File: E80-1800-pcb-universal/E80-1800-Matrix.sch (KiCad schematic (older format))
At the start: 276 parts

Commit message: finished pcb layout, added silk labels
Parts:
- D2001, D2002, D2003, D2004, D2005, D2006, D2007, D2008, D2009, D2010, D2011, D2012, D2013, D2014, D2015, D2016, D2017, D2018, D2019, D2020, D2021, D2022, D2023, D2024, D2025, D2026, D2027, D2028, D2029, D2030, D2031, D2032, D2033, D2034, D2035, D2036, D2037, D2038, D2039, D2040, D2041, D2042, D2043, D2044, D2045, D2046, D2047, D2048, D2049, D2050, D2051, D2052, D2053, D2054: LCSC (none) -> C68978
- R2001, R2002, R2003, R2004, R2005, R2006, R2007, R2008, R2009, R2010, R2011, R2012, R2013, R2014, R2015, R2016, R2017, R2018, R2019, R2020, R2021, R2022, R2023, R2024, R2025, R2026, R2027, R2028, R2029, R2030, R2031, R2032, R2033, R2034, R2035, R2036, R2037, R2038, R2039, R2040, R2041, R2042, R2043, R2044, R2045, R2046, R2047, R2048, R2049, R2050, R2051, R2052, R2053, R2054, R2055, R2056, R2057, R2058, R2059, R2060, R2061, R2062, R2063, R2064, R2065, R2066, R2067, R2068, R2069, R2070, R2071, R2072, R2073, R2074, R2075, R2076, R2077, R2078, R2079, R2080, R2081, R2082, R2083, R2084, R2085, R2086, R2087, R2088, R2089, R2090, R2091, R2092, R2093, R2094, R2095, R2096, R2097, R2098, R2099, R2100, R2101, R2102, R2103, R2104, R2105, R2106, R2107: LCSC (none) -> C23204

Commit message: improved mounting holes
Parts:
- renumbered D2007 to D10, D2008 to D11, D2009 to D12, D2010 to D13, D2011 to D14, D2012 to D15, D2013 to D16, D2014 to D17, D2015 to D18, D2016 to D19, D2017 to D20, D2018 to D21, D2019 to D22, D2020 to D23, D2021 to D24, D2022 to D25, D2023 to D26, D2024 to D27, D2025 to D28, D2026 to D29, D2027 to D30, D2028 to D31, D2029 to D32, D2030 to D33, D2031 to D34, D2032 to D35, D2033 to D36, D2034 to D37, D2035 to D38, D2036 to D39, D2001 to D4, D2037 to D40, D2038 to D41, D2039 to D42, D2040 to D43, D2041 to D44, D2042 to D45, D2043 to D46, D2044 to D47, D2045 to D48, D2046 to D49, D2002 to D5, D2047 to D50, D2048 to D51, D2049 to D52, D2050 to D53, D2051 to D54, D2052 to D55, D2053 to D56, D2054 to D57, D2003 to D6, D2004 to D7, D2005 to D8, D2006 to D9, MX2001 to MX1, MX2010 to MX10, MX2100 to MX100, MX2101 to MX101, MX2102 to MX102, MX2103 to MX103, MX2104 to MX104, MX2105 to MX105, MX2106 to MX106, MX2107 to MX107, MX2108 to MX108, MX2109 to MX109, MX2011 to MX11, MX2110 to MX110, MX2111 to MX111, MX2112 to MX112, MX2113 to MX113, MX2114 to MX114, MX2115 to MX115, MX2012 to MX12, MX2013 to MX13, MX2014 to MX14, MX2015 to MX15, MX2016 to MX16, MX2017 to MX17, MX2018 to MX18, MX2019 to MX19, MX2002 to MX2, MX2020 to MX20, MX2021 to MX21, MX2022 to MX22, MX2023 to MX23, MX2024 to MX24, MX2025 to MX25, MX2026 to MX26, MX2027 to MX27, MX2028 to MX28, MX2029 to MX29, MX2003 to MX3, MX2030 to MX30, MX2031 to MX31, MX2032 to MX32, MX2033 to MX33, MX2034 to MX34, MX2035 to MX35, MX2036 to MX36, MX2037 to MX37, MX2038 to MX38, MX2039 to MX39, MX2004 to MX4, MX2040 to MX40, MX2041 to MX41, MX2042 to MX42, MX2043 to MX43, MX2044 to MX44, MX2045 to MX45, MX2046 to MX46, MX2047 to MX47, MX2048 to MX48, MX2049 to MX49, MX2005 to MX5, MX2050 to MX50, MX2051 to MX51, MX2052 to MX52, MX2053 to MX53, MX2054 to MX54, MX2055 to MX55, MX2056 to MX56, MX2057 to MX57, MX2058 to MX58, MX2059 to MX59, MX2006 to MX6, MX2060 to MX60, MX2061 to MX61, MX2062 to MX62, MX2063 to MX63, MX2064 to MX64, MX2065 to MX65, MX2066 to MX66, MX2067 to MX67, MX2068 to MX68, MX2069 to MX69, MX2007 to MX7, MX2070 to MX70, MX2071 to MX71, MX2072 to MX72, MX2073 to MX73, MX2074 to MX74, MX2075 to MX75, MX2076 to MX76, MX2077 to MX77, MX2078 to MX78, MX2079 to MX79, MX2008 to MX8, MX2080 to MX80, MX2081 to MX81, MX2082 to MX82, MX2083 to MX83, MX2084 to MX84, MX2085 to MX85, MX2086 to MX86, MX2087 to MX87, MX2088 to MX88, MX2089 to MX89, MX2009 to MX9, MX2090 to MX90, MX2091 to MX91, MX2092 to MX92, MX2093 to MX93, MX2094 to MX94, MX2095 to MX95, MX2096 to MX96, MX2097 to MX97, MX2098 to MX98, MX2099 to MX99, R2086 to R100, R2087 to R101, R2088 to R102, R2089 to R103, R2090 to R104, R2091 to R105, R2092 to R106, R2093 to R107, R2094 to R108, R2095 to R109, R2096 to R110, R2097 to R111, R2098 to R112, R2099 to R113, R2100 to R114, R2101 to R115, R2102 to R116, R2103 to R117, R2104 to R118, R2105 to R119, R2106 to R120, R2107 to R121, R2001 to R15, R2002 to R16, R2003 to R17, R2004 to R18, R2005 to R19, R2006 to R20, R2007 to R21, R2008 to R22, R2009 to R23, R2010 to R24, R2011 to R25, R2012 to R26, R2013 to R27, R2014 to R28, R2015 to R29, R2016 to R30, R2017 to R31, R2018 to R32, R2019 to R33, R2020 to R34, R2021 to R35, R2022 to R36, R2023 to R37, R2024 to R38, R2025 to R39, R2026 to R40, R2027 to R41, R2028 to R42, R2029 to R43, R2030 to R44, R2031 to R45, R2032 to R46, R2033 to R47, R2034 to R48, R2035 to R49, R2036 to R50, R2037 to R51, R2038 to R52, R2039 to R53, R2040 to R54, R2041 to R55, R2042 to R56, R2043 to R57, R2044 to R58, R2045 to R59, R2046 to R60, R2047 to R61, R2048 to R62, R2049 to R63, R2050 to R64, R2051 to R65, R2052 to R66, R2053 to R67, R2054 to R68, R2055 to R69, R2056 to R70, R2057 to R71, R2058 to R72, R2059 to R73, R2060 to R74, R2061 to R75, R2062 to R76, R2063 to R77, R2064 to R78, R2065 to R79, R2066 to R80, R2067 to R81, R2068 to R82, R2069 to R83, R2070 to R84, R2071 to R85, R2072 to R86, R2073 to R87, R2074 to R88, R2075 to R89, R2076 to R90, R2077 to R91, R2078 to R92, R2079 to R93, R2080 to R94, R2081 to R95, R2082 to R96, R2083 to R97, R2084 to R98, R2085 to R99

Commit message: minor routing changes
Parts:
- D10, D11, D12, D13, D14, D15, D16, D17, D18, D19, D20, D21, D22, D23, D24, D25, D26, D27, D28, D29, D30, D31, D32, D33, D34, D35, D36, D37, D38, D39, D4, D40, D41, D42, D43, D44, D45, D46, D47, D48, D49, D5, D50, D51, D52, D53, D54, D55, D56, D57, D6, D7, D8, D9: footprint Package_TO_SOT_SMD:SOT-23 -> kicad-keyboard-parts:SOT-23_stealth
- R100, R101, R102, R103, R104, R105, R106, R107, R108, R109, R110, R111, R112, R113, R114, R115, R116, R117, R118, R119, R120, R121, R15, R16, R17, R18, R19, R20, R21, R22, R23, R24, R25, R26, R27, R28, R29, R30, R31, R32, R33, R34, R35, R36, R37, R38, R39, R40, R41, R42, R43, R44, R45, R46, R47, R48, R49, R50, R51, R52, R53, R54, R55, R56, R57, R58, R59, R60, R61, R62, R63, R64, R65, R66, R67, R68, R69, R70, R71, R72, R73, R74, R75, R76, R77, R78, R79, R80, R81, R82, R83, R84, R85, R86, R87, R88, R89, R90, R91, R92, R93, R94, R95, R96, R97, R98, R99: footprint Resistor_SMD:R_0603_1608Metric_Pad1.05x0.95mm_HandSolder -> kicad-keyboard-parts:R_0603_1608Metric_stealth

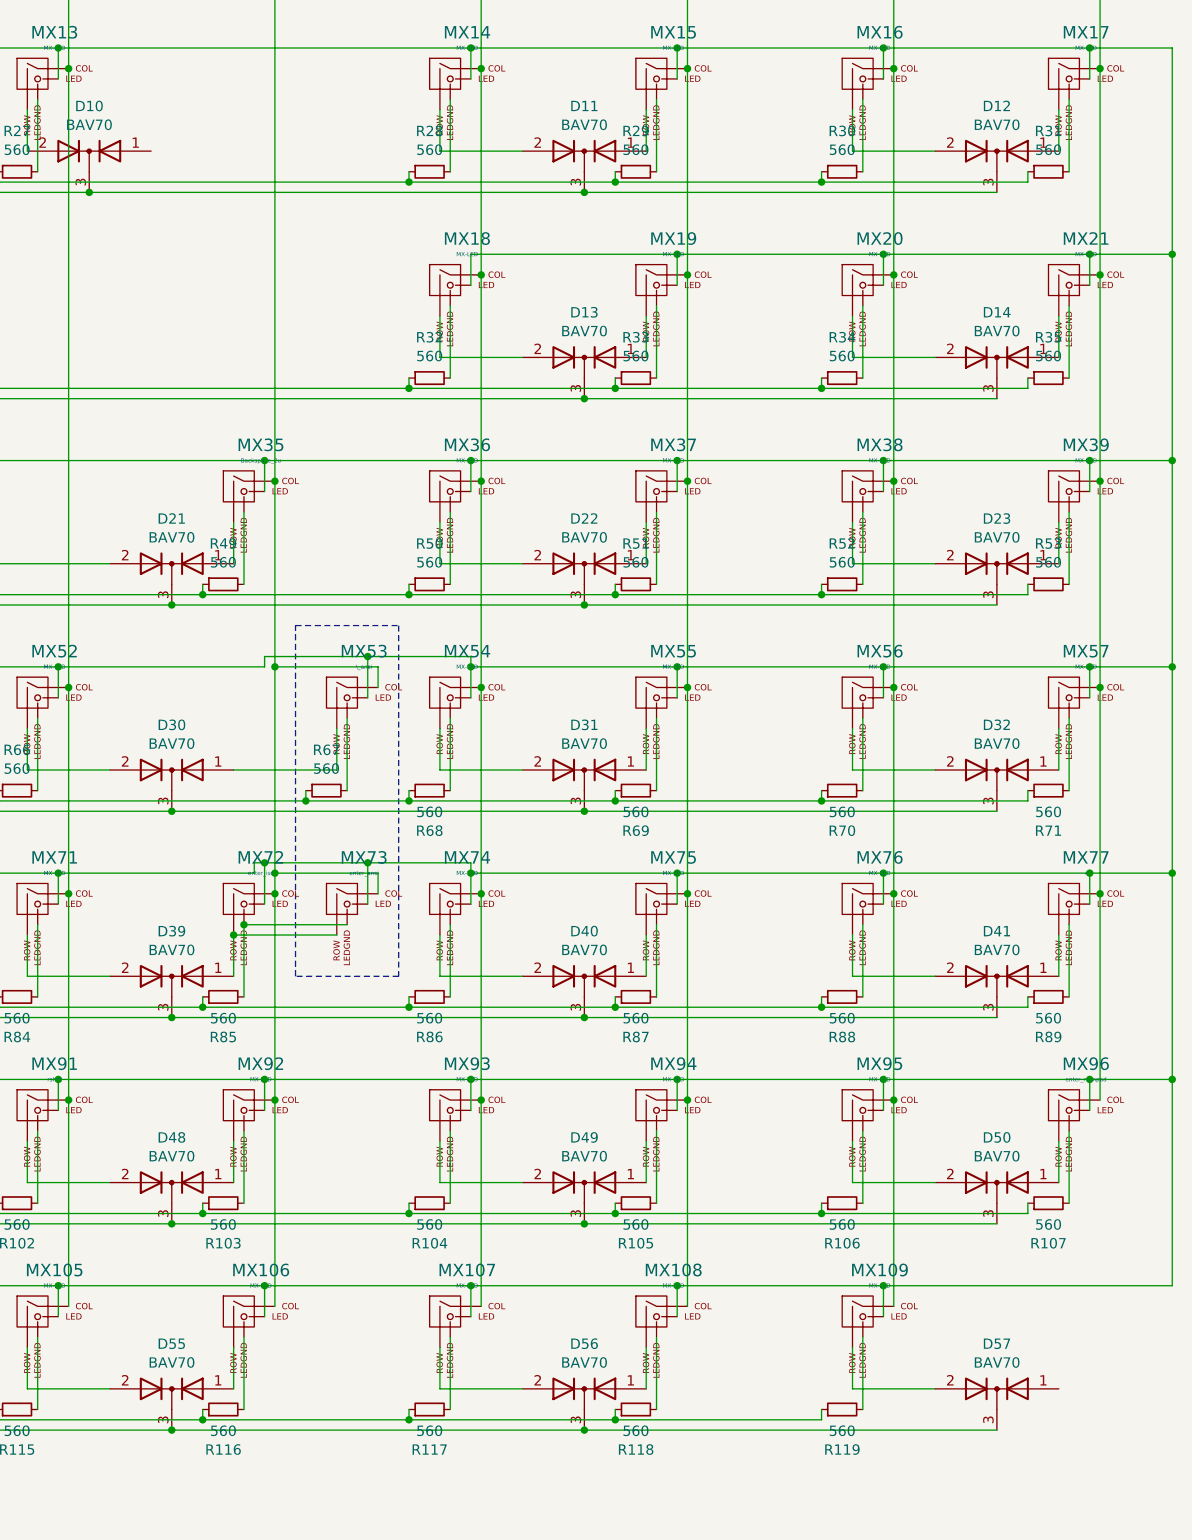
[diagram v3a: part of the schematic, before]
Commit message: increased readability, added missing cap
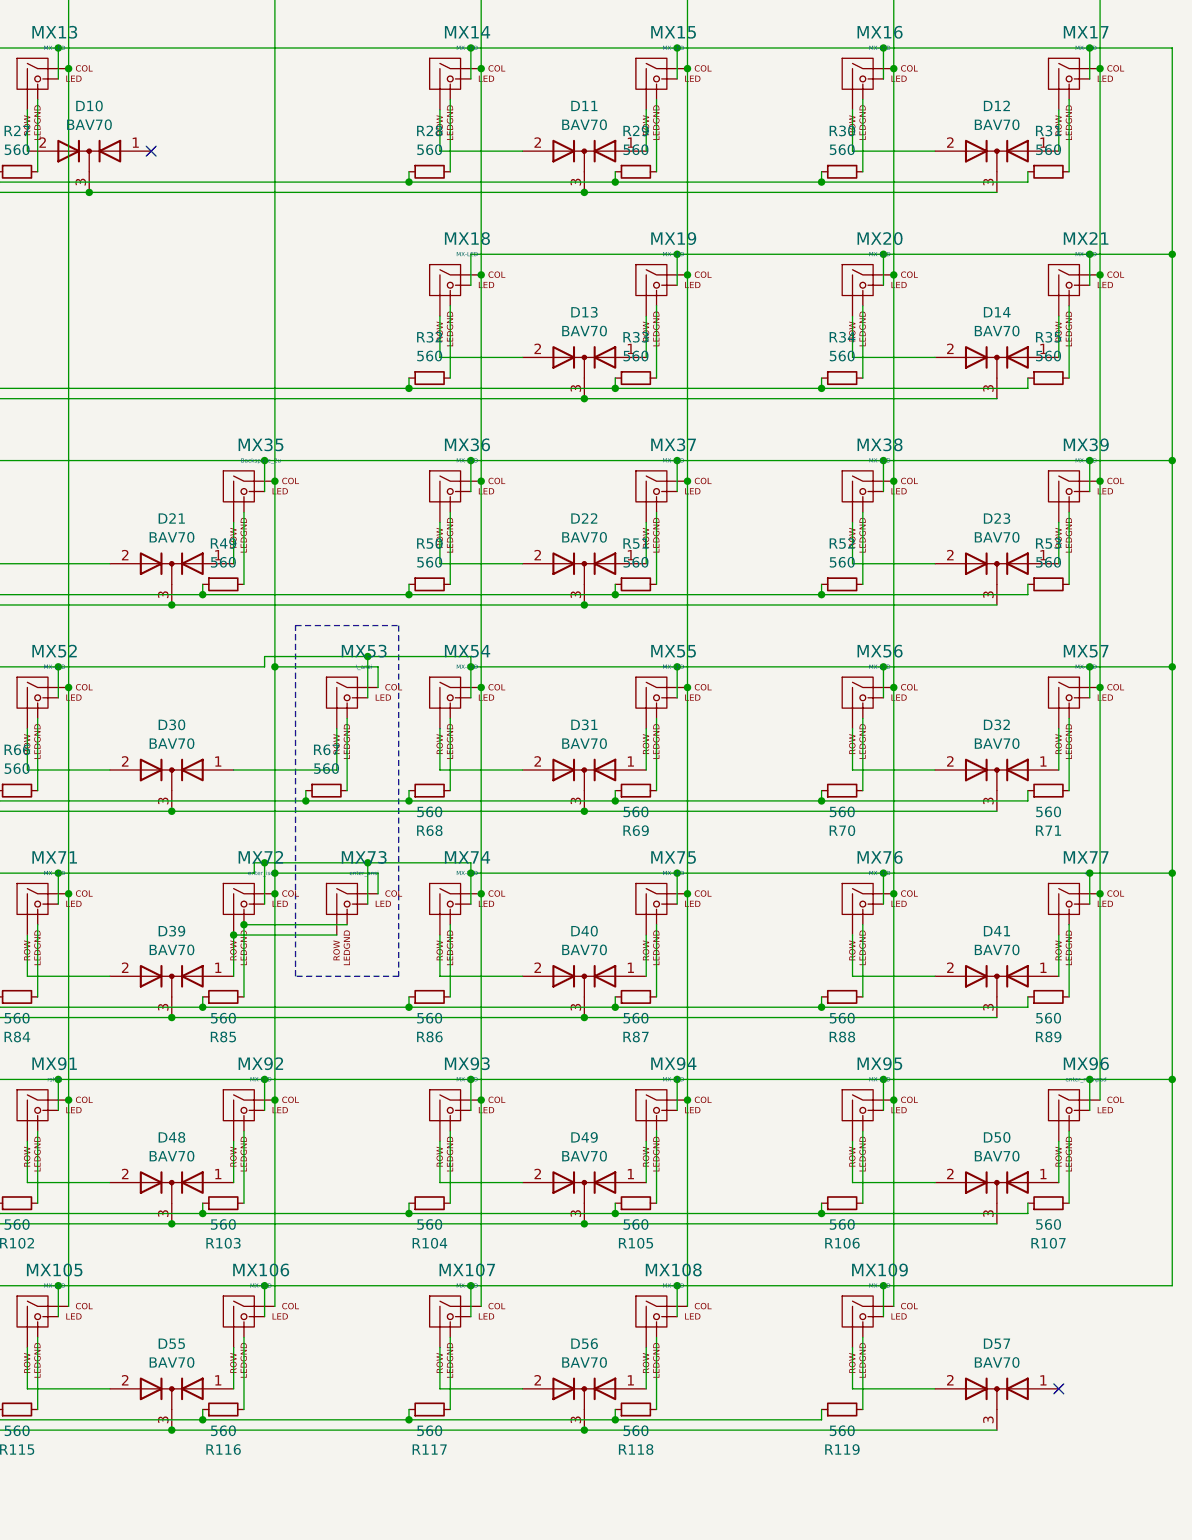
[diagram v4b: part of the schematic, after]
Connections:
- no-connect marks 0 -> 2
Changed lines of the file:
@@
 Connection ~ 20100 2350
 $Comp
-L power:+5V #PWR022
+L power:+5V #PWR028
 U 1 1 649944E0
 P 1200 2350
-F 0 "#PWR022" H 1200 2200 50  0001 C CNN
+F 0 "#PWR028" H 1200 2200 50  0001 C CNN
 F 1 "+5V" H 1215 2523 50  0000 C CNN
 F 2 "" H 1200 2350 50  0001 C CNN
@@
 Wire Wire Line
 	2150 6300 2150 6450
+NoConn ~ 19950 8850
+NoConn ~ 15550 2850
 $EndSCHEMATC

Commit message: added TVS for ESD prot
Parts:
- renumbered D9 to D10, D10 to D11, D11 to D12, D12 to D13, D13 to D14, D14 to D15, D15 to D16, D16 to D17, D17 to D18, D18 to D19, D19 to D20, D20 to D21, D21 to D22, D22 to D23, D23 to D24, D24 to D25, D25 to D26, D26 to D27, D27 to D28, D28 to D29, D29 to D30, D30 to D31, D31 to D32, D32 to D33, D33 to D34, D34 to D35, D35 to D36, D36 to D37, D37 to D38, D38 to D39, D39 to D40, D40 to D41, D41 to D42, D42 to D43, D43 to D44, D44 to D45, D45 to D46, D46 to D47, D47 to D48, D48 to D49, D4 to D5, D49 to D50, D50 to D51, D51 to D52, D52 to D53, D53 to D54, D54 to D55, D55 to D56, D56 to D57, D57 to D58, D5 to D6, D6 to D7, D7 to D8, D8 to D9
